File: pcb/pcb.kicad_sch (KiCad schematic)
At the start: 33 parts, among them J1 NMJ4HCD2, J2 NMJ4HCD2, U1 RC4558

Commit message: add 3pdt footprint and symbol
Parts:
- added SW1: ~, 3PDT:SW_3PDT_GENERIC, symbol 3PDT:SW_3PDT
- J1, J2: footprint NMJ4HCD2:NMJ4HCD2 -> NMJ4HCD2
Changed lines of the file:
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@@
 			)
 		)
-		(property "Footprint" "NMJ4HCD2:NMJ4HCD2"
+		(property "Footprint" "NMJ4HCD2"
 			(at 24.13 211.76 0)
 			(effects
@@
 	)
 	(symbol
+		(lib_id "3PDT:SW_3PDT")
+		(at 127 177.8 0)
+		(unit 1)
+		(exclude_from_sim no)
+		(in_bom yes)
+		(on_board yes)
+		(dnp no)
+		(fields_autoplaced yes)
+		(property "Reference" "SW1"
+			(at 127 180.34 0)
+			(effects
+				(font
+					(size 1.27 1.27)
+				)
+			)
+		)
+		(property "Value" "~"
+			(at 127 182.88 0)
+			(effects
+				(font
+					(size 1.27 1.27)
+				)
+			)
+		)
+		(property "Footprint" "3PDT:SW_3PDT_GENERIC"
+			(at 127 177.8 0)
+			(effects
+				(font
+					(size 1.27 1.27)
+				)
+				(hide yes)
+			)
+		)
+		(property "Datasheet" ""
+			(at 127 177.8 0)
+			(effects
+				(font
+					(size 1.27 1.27)
+				)
+				(hide yes)
+			)
+		)
+		(property "Description" ""
+			(at 127 177.8 0)
+			(effects
+				(font
+					(size 1.27 1.27)
+				)
+				(hide yes)
+			)
+		)
+		(pin "2"
+		)
+		(pin "7"
+		)
+		(pin "1"
+		)
+		(pin "9"
+		)
+		(pin "4"
+		)
+		(pin "3"
+		)
+		(pin "6"
+		)
+		(pin "8"
+		)
+		(pin "5"
+		)
+		(instances
+			(project ""
+				(path "/0709eb16-b1b4-4efb-9d5a-efabba183f02"
+					(reference "SW1")
+					(unit 1)
+				)
+			)
+		)
+	)
+	(symbol
 		(lib_id "Device:C")
 		(at 107.95 107.95 180)
@@
 			)
 		)
-		(property "Footprint" "NMJ4HCD2:NMJ4HCD2"
+		(property "Footprint" "NMJ4HCD2"
 			(at 24.13 163.5 0)
 			(effects

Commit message: FIX LIBRARIES :O
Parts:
- J1, J2: footprint NMJ4HCD2 -> NMJ4HCD2:NMJ4HCD2
- SW1: value ~ -> FSWITCH; footprint 3PDT:SW_3PDT_GENERIC -> 3PDT:3PDT
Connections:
- net GND: now also SW1.1, SW1.2, SW1.5
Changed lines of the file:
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@@
+	)
+	(symbol
+		(lib_id "power:GND")
+		(at 106.68 160.02 180)
+		(unit 1)
+		(exclude_from_sim no)
+		(in_bom yes)
+		(on_board yes)
+		(dnp no)
+		(fields_autoplaced yes)
+		(property "Reference" "#PWR013"
+			(at 106.68 153.67 0)
+			(effects
+				(font
+					(size 1.27 1.27)
+				)
+				(hide yes)
+			)
+		)
+		(property "Value" "GND"
+			(at 106.68 154.94 0)
+			(effects
+				(font
+					(size 1.27 1.27)
+				)
+			)
+		)
+		(property "Footprint" ""
+			(at 106.68 160.02 0)
+			(effects
+				(font
+					(size 1.27 1.27)
+				)
+				(hide yes)
+			)
+		)
+		(property "Datasheet" ""
+			(at 106.68 160.02 0)
+			(effects
+				(font
+					(size 1.27 1.27)
+				)
+				(hide yes)
+			)
+		)
+		(property "Description" "Power symbol creates a global label with name \"GND\" , ground"
+			(at 106.68 160.02 0)
+			(effects
+				(font
+					(size 1.27 1.27)
+				)
+				(hide yes)
+			)
+		)
+		(pin "1"
+		)
+		(instances
+			(project ""
+				(path "/0709eb16-b1b4-4efb-9d5a-efabba183f02"
+					(reference "#PWR013")
+					(unit 1)
+				)
+			)
+		)
 	)
 	(symbol
@@
 			)
 		)
-		(property "Footprint" "NMJ4HCD2"
+		(property "Footprint" "NMJ4HCD2:NMJ4HCD2"
 			(at 24.13 211.76 0)
 			(effects
@@
 	(symbol
 		(lib_id "power:GND")
+		(at 111.76 160.02 180)
+		(unit 1)
+		(exclude_from_sim no)
+		(in_bom yes)
+		(on_board yes)
+		(dnp no)
+		(fields_autoplaced yes)
+		(property "Reference" "#PWR014"
+			(at 111.76 153.67 0)
+			(effects
+				(font
+					(size 1.27 1.27)
+				)
+				(hide yes)
+			)
+		)
+		(property "Value" "GND"
+			(at 111.76 154.94 0)
+			(effects
+				(font
+					(size 1.27 1.27)
+				)
+			)
+		)
+		(property "Footprint" ""
+			(at 111.76 160.02 0)
+			(effects
+				(font
+					(size 1.27 1.27)
+				)
+				(hide yes)
+			)
+		)
+		(property "Datasheet" ""
+			(at 111.76 160.02 0)
+			(effects
+				(font
+					(size 1.27 1.27)
+				)
+				(hide yes)
+			)
+		)
+		(property "Description" "Power symbol creates a global label with name \"GND\" , ground"
+			(at 111.76 160.02 0)
+			(effects
+				(font
+					(size 1.27 1.27)
+				)
+				(hide yes)
+			)
+		)
+		(pin "1"
+		)
+		(instances
+			(project "pcb"
+				(path "/0709eb16-b1b4-4efb-9d5a-efabba183f02"
+					(reference "#PWR014")
+					(unit 1)
+				)
+			)
+		)
+	)
+	(symbol
+		(lib_id "power:GND")
 		(at 209.55 38.1 0)
 		(unit 1)
@@
 			)
 		)
-		(property "Value" "~"
+		(property "Value" "FSWITCH"
 			(at 127 182.88 0)
 			(effects
@@
 			)
 		)
-		(property "Footprint" "3PDT:SW_3PDT_GENERIC"
+		(property "Footprint" "3PDT:3PDT"
 			(at 127 177.8 0)
 			(effects
@@
 				(path "/0709eb16-b1b4-4efb-9d5a-efabba183f02"
 					(reference "C1")
+					(unit 1)
+				)
+			)
+		)
+	)
+	(symbol
+		(lib_id "power:GND")
+		(at 127 160.02 180)
+		(unit 1)
+		(exclude_from_sim no)
+		(in_bom yes)
+		(on_board yes)
+		(dnp no)
+		(fields_autoplaced yes)
+		(property "Reference" "#PWR015"
+			(at 127 153.67 0)
+			(effects
+				(font
+					(size 1.27 1.27)
+				)
+				(hide yes)
+			)
+		)
+		(property "Value" "GND"
+			(at 127 154.94 0)
+			(effects
+				(font
+					(size 1.27 1.27)
+				)
+			)
+		)
+		(property "Footprint" ""
+			(at 127 160.02 0)
+			(effects
+				(font
+					(size 1.27 1.27)
+				)
+				(hide yes)
+			)
+		)
+		(property "Datasheet" ""
+			(at 127 160.02 0)
+			(effects
+				(font
+					(size 1.27 1.27)
+				)
+				(hide yes)
+			)
+		)
+		(property "Description" "Power symbol creates a global label with name \"GND\" , ground"
+			(at 127 160.02 0)
+			(effects
+				(font
+					(size 1.27 1.27)
+				)
+				(hide yes)
+			)
+		)
+		(pin "1"
+		)
+		(instances
+			(project "pcb"
+				(path "/0709eb16-b1b4-4efb-9d5a-efabba183f02"
+					(reference "#PWR015")
 					(unit 1)
 				)
@@
 			)
 		)
-		(property "Footprint" "NMJ4HCD2"
+		(property "Footprint" "NMJ4HCD2:NMJ4HCD2"
 			(at 24.13 163.5 0)
 			(effects

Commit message: Finalize pcb
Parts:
- added C14: 100n, Capacitor_THT:C_Rect_L7.2mm_W2.5mm_P5.00mm, symbol Device:C
- added D5: LED, LED_THT:LED_D3.0mm, symbol Device:LED
- added R12, R13, R14, R7: 1k, Resistor_THT:R_Axial_DIN0207_L6.3mm_D2.5mm_P10.16mm_Horizontal, symbol Device:R
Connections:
- net AMP1-: now also RV1.3; no longer RV1.1
- net AMP1OUT: now also R12.2; no longer RV1.2
- net GND: now also RV3.3, SW1.6, C14.1, D5.1 (K); no longer RV3.1, SW1.1, SW1.2, SW1.5
- net VCC: now also SW1.4, C14.2
- net VCLIP: now also R13.1; no longer RV2.1
- net VIN: now also SW1.2; no longer C4.1, R4.1
- net VOUT: now also SW1.8; no longer RV3.2
- net at SW1.3: now also SW1.9
- net VVOLOUT: now reaches SW1.7
- net VVOLOUT: now also RV3.2
- net at C13.2: now also R14.1; no longer RV3.3
- net at RV2.3: now also R13.2
- new net: R12.1, RV1.2
- new net: R7.2, SW1.5
- new net: D5.2 (A), R7.1
- new net: R14.2, RV3.1
- new net VAMPIN: C4.1, R4.1, SW1.1
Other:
- note added: "TODO: power supply barrel jack"
- note removed: "TODO: power supply barrel jack, stomp switch bypass, drill holes?"
- moved on the sheet: C13, RV1, RV2, RV3, SW1

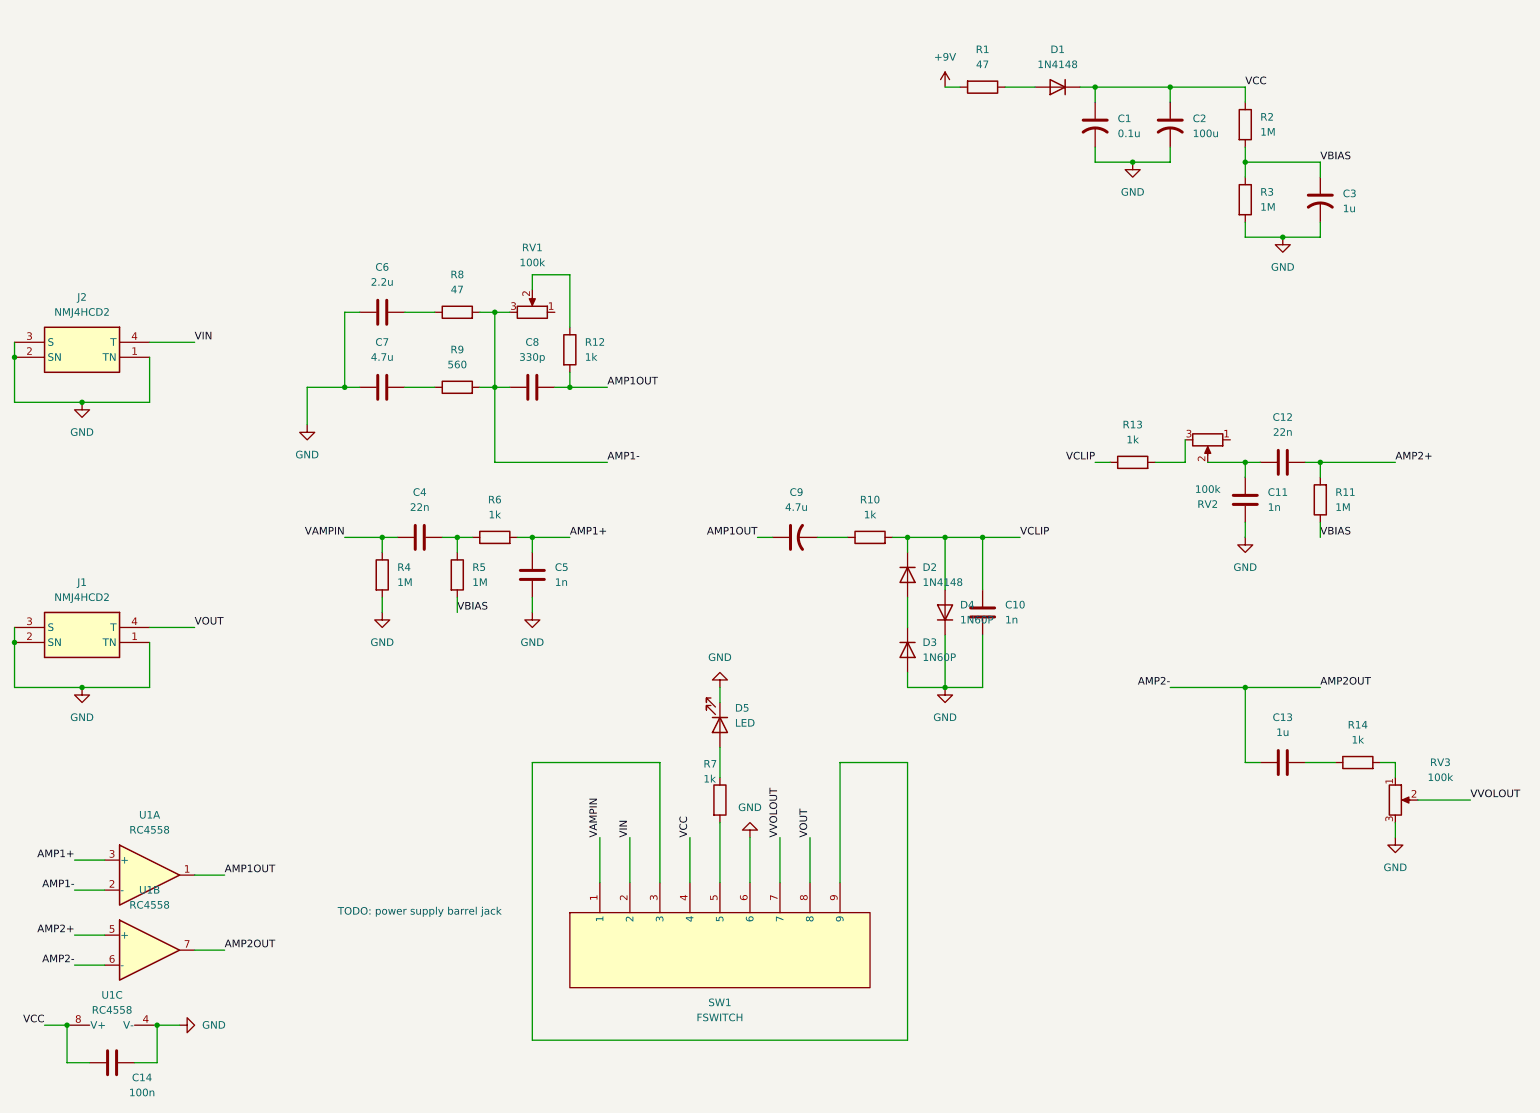
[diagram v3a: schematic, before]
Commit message: Rework Amplifier Stage
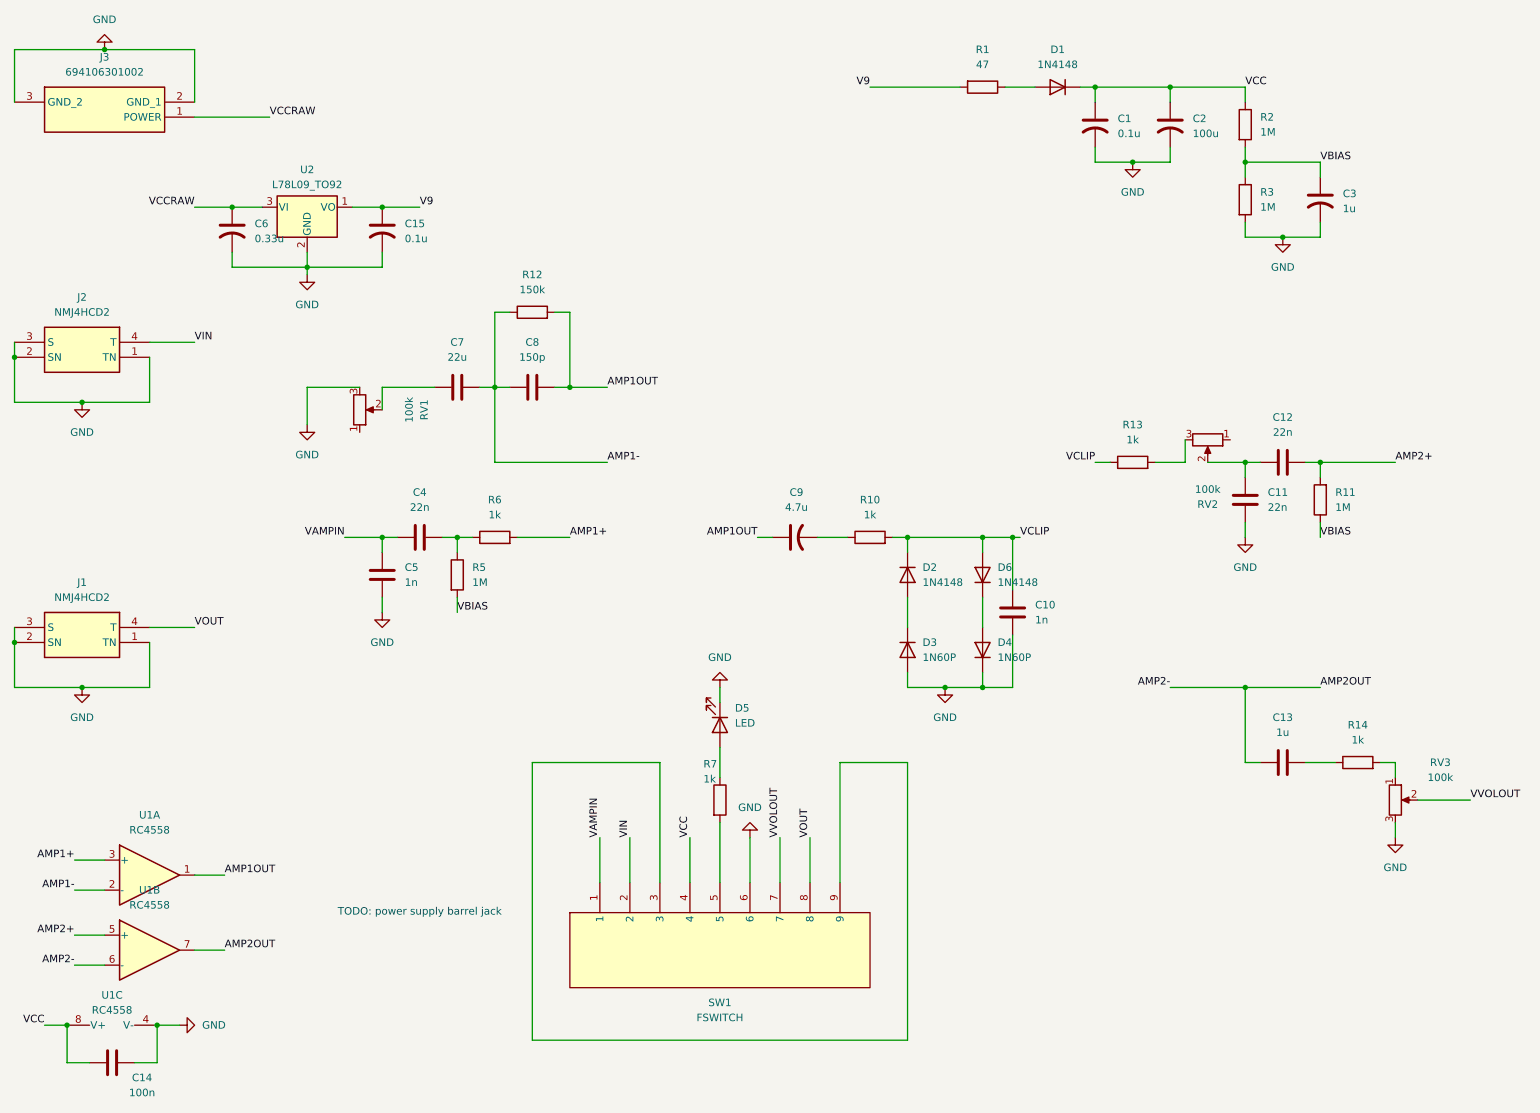
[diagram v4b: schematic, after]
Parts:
- removed C6: 2.2u, Capacitor_THT:C_Radial_D5.0mm_H11.0mm_P2.00mm, symbol Device:C
- removed R4: 1M, Resistor_THT:R_Axial_DIN0207_L6.3mm_D2.5mm_P10.16mm_Horizontal, symbol Device:R
- removed R8: 47, Resistor_THT:R_Axial_DIN0207_L6.3mm_D2.5mm_P10.16mm_Horizontal, symbol Device:R
- removed R9: 560, Resistor_THT:R_Axial_DIN0207_L6.3mm_D2.5mm_P10.16mm_Horizontal, symbol Device:R
- added C15: 0.1u, Capacitor_THT:C_Radial_D5.0mm_H11.0mm_P2.00mm, symbol Device:C_US
- added C6: 0.33u, Capacitor_THT:C_Radial_D5.0mm_H11.0mm_P2.00mm, symbol Device:C_US
- added D6: 1N4148, Diode_THT:D_DO-35_SOD27_P7.62mm_Horizontal, symbol Device:D
- added J3: 694106301002, PowerJackFemale:694106301002, symbol PowerJackFemale:694106301002
- added U2: L78L09_TO92, Package_TO_SOT_THT:TO-92_Inline, symbol Regulator_Linear:L78L09_TO92
- C11: value 1n -> 22n
- C14: footprint Capacitor_THT:C_Rect_L7.2mm_W2.5mm_P5.00mm -> Capacitor_THT:C_Disc_D3.0mm_W1.6mm_P2.50mm
- C7: value 4.7u -> 22u
- C8: value 330p -> 150p; footprint Capacitor_THT:C_Disc_D4.3mm_W1.9mm_P5.00mm -> Capacitor_THT:C_Disc_D3.0mm_W1.6mm_P2.50mm
- R12: value 1k -> 150k
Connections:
- net AMP1+: no longer C5.2
- net AMP1-: now also C7.2, R12.1; no longer RV1.3
- net GND: now also RV1.3, C15.2, C6.2, J3.2 (GND_1), J3.3 (GND_2), U2.2 (GND); no longer C7.1
- net VAMPIN: now also C5.2
- net VCLIP: now also D6.2 (A); no longer D4.2 (A)
- net at RV1.2: now also C7.1; no longer R12.1
- net +9V renamed V9
- net V9: now also C15.1, U2.1 (VO)
- new net: D4.2 (A), D6.1 (K)
- new net VCCRAW: C6.1, J3.1 (POWER), U2.3 (VI)
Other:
- moved on the sheet: C10, C5, C7, D4, R12, RV1

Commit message: Finalize pcb
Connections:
- net GND: now also RV1.1, RV2.1, RV3.1; no longer RV3.3
- net at R14.2: now also RV3.3; no longer RV3.1
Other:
- note removed: "TODO: power supply barrel jack"
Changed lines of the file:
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@@
 	(generator_version "9.0")
 	(paper "A4")
-	(text "TODO: power supply barrel jack"
-		(exclude_from_sim yes)
-		(at 88.9 165.1 0)
-		(effects
-			(font
-				(size 1.27 1.27)
-			)
-		)
-	)
 	(junction
 		(at 177.8 127)
@@
 	(symbol
 		(lib_id "power:GND")
+		(at 226.06 85.09 90)
+		(unit 1)
+		(exclude_from_sim no)
+		(in_bom yes)
+		(on_board yes)
+		(dnp no)
+		(fields_autoplaced yes)
+		(property "Reference" "#PWR016"
+			(at 232.41 85.09 0)
+			(effects
+				(font
+					(size 1.27 1.27)
+				)
+				(hide yes)
+			)
+		)
+		(property "Value" "GND"
+			(at 229.87 85.0899 90)
+			(effects
+				(font
+					(size 1.27 1.27)
+				)
+				(justify right)
+			)
+		)
+		(property "Footprint" ""
+			(at 226.06 85.09 0)
+			(effects
+				(font
+					(size 1.27 1.27)
+				)
+				(hide yes)
+			)
+		)
+		(property "Datasheet" ""
+			(at 226.06 85.09 0)
+			(effects
+				(font
+					(size 1.27 1.27)
+				)
+				(hide yes)
+			)
+		)
+		(property "Description" "Power symbol creates a global label with name \"GND\" , ground"
+			(at 226.06 85.09 0)
+			(effects
+				(font
+					(size 1.27 1.27)
+				)
+				(hide yes)
+			)
+		)
+		(pin "1"
+		)
+		(instances
+			(project "pcb"
+				(path "/0709eb16-b1b4-4efb-9d5a-efabba183f02"
+					(reference "#PWR016")
+					(unit 1)
+				)
+			)
+		)
+	)
+	(symbol
+		(lib_id "power:GND")
+		(at 78.74 83.82 0)
+		(unit 1)
+		(exclude_from_sim no)
+		(in_bom yes)
+		(on_board yes)
+		(dnp no)
+		(fields_autoplaced yes)
+		(property "Reference" "#PWR08"
+			(at 78.74 90.17 0)
+			(effects
+				(font
+					(size 1.27 1.27)
+				)
+				(hide yes)
+			)
+		)
+		(property "Value" "GND"
+			(at 78.74 88.9 0)
+			(effects
+				(font
+					(size 1.27 1.27)
+				)
+			)
+		)
+		(property "Footprint" ""
+			(at 78.74 83.82 0)
+			(effects
+				(font
+					(size 1.27 1.27)
+				)
+				(hide yes)
+			)
+		)
+		(property "Datasheet" ""
+			(at 78.74 83.82 0)
+			(effects
+				(font
+					(size 1.27 1.27)
+				)
+				(hide yes)
+			)
+		)
+		(property "Description" "Power symbol creates a global label with name \"GND\" , ground"
+			(at 78.74 83.82 0)
+			(effects
+				(font
+					(size 1.27 1.27)
+				)
+				(hide yes)
+			)
+		)
+		(pin "1"
+		)
+		(instances
+			(project ""
+				(path "/0709eb16-b1b4-4efb-9d5a-efabba183f02"
+					(reference "#PWR08")
+					(unit 1)
+				)
+			)
+		)
+	)
+	(symbol
+		(lib_id "power:GND")
 		(at 35.56 19.05 180)
 		(unit 1)
@@
 		(lib_id "Device:R_Potentiometer")
 		(at 78.74 80.01 0)
-		(mirror x)
 		(unit 1)
 		(exclude_from_sim no)
@@
 		(lib_id "Device:R_Potentiometer")
 		(at 254 146.05 0)
+		(mirror x)
 		(unit 1)
 		(exclude_from_sim no)
@@
 		(dnp no)
 		(property "Reference" "RV3"
-			(at 261.62 139.7 0)
+			(at 261.62 152.4 0)
 			(effects
 				(font
@@
 		)
 		(property "Value" "100k"
-			(at 261.62 142.24 0)
+			(at 261.62 149.86 0)
 			(effects
 				(font
